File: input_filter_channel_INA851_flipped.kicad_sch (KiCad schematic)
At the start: 28 parts, among them K1 EE2-12TNU-L, U101 INA851

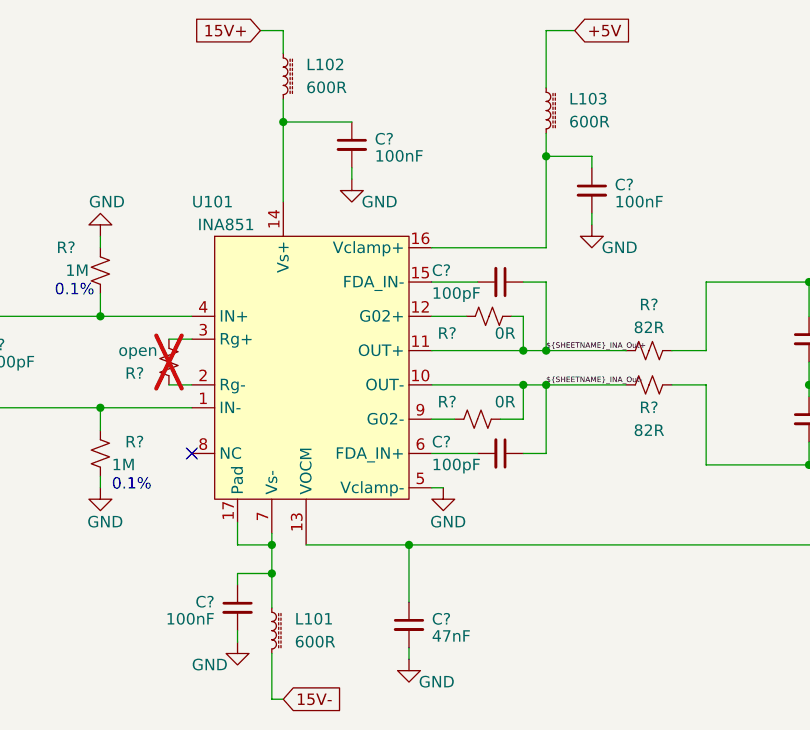
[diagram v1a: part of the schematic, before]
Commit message: Updated Project
Schematics:
-updated level shifting IC's
-Add notes to level shifters
-Changed Relay Coil Driver channel mapping
-Added additional Mounting Hole

Layout
-WIP To Complete:
-Relay Driver ICs
- Reworking LT8582 area
- Level Shifters
- Housekeeping ICs
-Misc. error cleanup
- Silkscreen adjust
- Add Silkscreen SN & logo
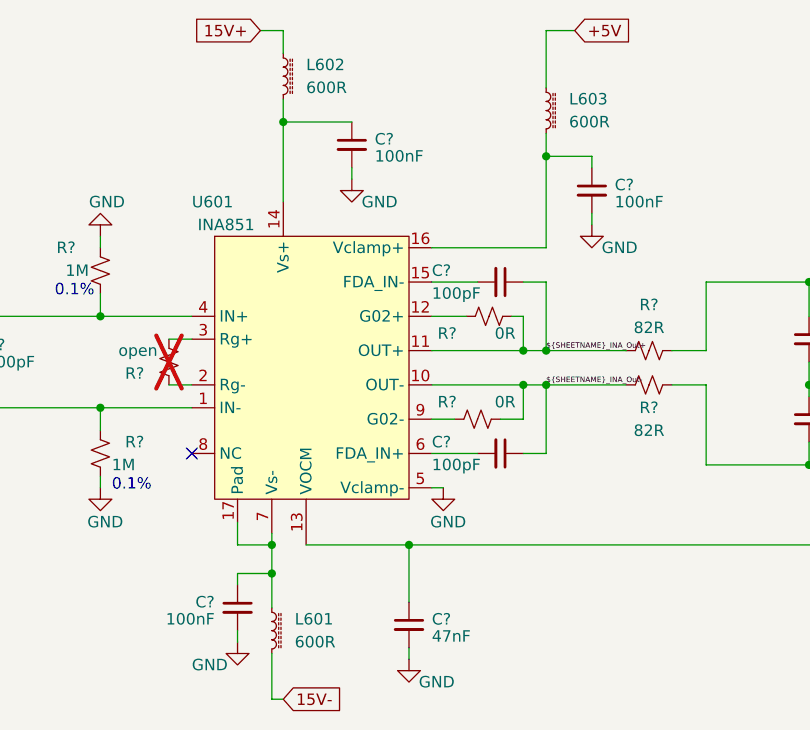
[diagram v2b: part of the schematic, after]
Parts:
- renumbered L101 to L601, L102 to L602, L103 to L603, U101 to U601

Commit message: Updated Project with Latest Changes
Project:
-Added pdf plots of PCB layout

Schematics:
-Fixed L8 Pinout
-Adjusted FMC connections
-Adjusted level shifter connections

Layout:
-Completed AFE/ADC/Power/Relay driver sections

Layout WIP To Complete:
-Misc. error cleanup
- Silkscreen adjust
- Add Silkscreen SN & logo
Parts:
- U601: footprint Package_DFN_QFN:QFN-16-1EP_3x3mm_P0.5mm_EP1.75x1.75mm_ThermalVias -> footprints:QFN-16-1EP_3x3mm_P0.5mm_EP1.75x1.75mm_ThermalVias
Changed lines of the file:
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@@
       (effects (font (size 1.27 1.27)))
     )
-    (property "Footprint" "Package_DFN_QFN:QFN-16-1EP_3x3mm_P0.5mm_EP1.75x1.75mm_ThermalVias" (at 147.32 77.47 0)
+    (property "Footprint" "footprints:QFN-16-1EP_3x3mm_P0.5mm_EP1.75x1.75mm_ThermalVias" (at 147.32 77.47 0)
       (effects (font (size 1.27 1.27)) hide)
     )

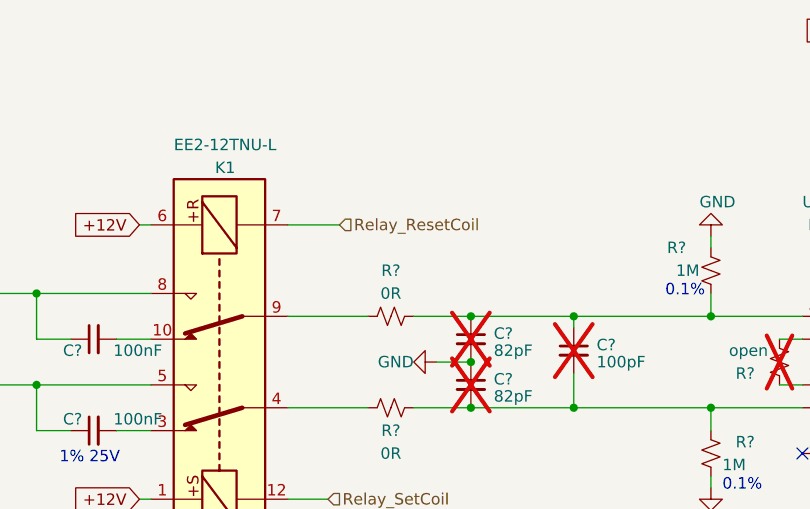
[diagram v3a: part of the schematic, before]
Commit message: Push Version before ADC change from 1.8V to 2.5V I/O
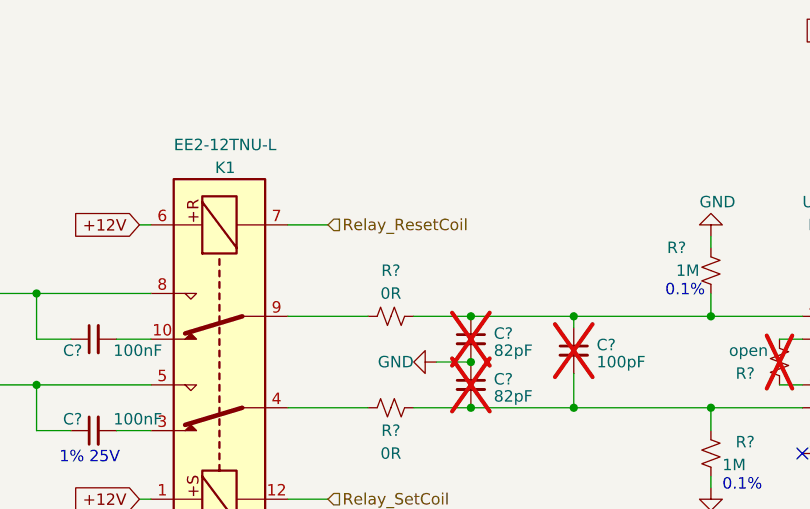
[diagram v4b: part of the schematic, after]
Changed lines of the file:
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@@
     (stroke (width 0) (type default))
   )
-  (wire (pts (xy 87.63 76.2) (xy 93.345 76.2))
+  (wire (pts (xy 87.63 76.2) (xy 92.075 76.2))
     (stroke (width 0) (type default))
   )
@@
     )
   )
-  (hierarchical_label "Relay_ResetCoil" (shape input) (at 93.345 76.2 0) (fields_autoplaced)
+  (hierarchical_label "Relay_ResetCoil" (shape input) (at 92.075 76.2 0) (fields_autoplaced)
     (effects (font (size 1.27 1.27)) (justify left))
   )
